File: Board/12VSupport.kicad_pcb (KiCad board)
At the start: 2 copper layers, 106.7 x 123.2 mm, 87 parts, among them J1 12V, J2 BATT, J3 BUCK_IN, J4 BUCK_OUT, J5 BOOST_IN, J6 BOOST_OUT, J7 TMP36GZ, J8 HEATER, J9 ICSP, K1 SLA-05VDC-SL-C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

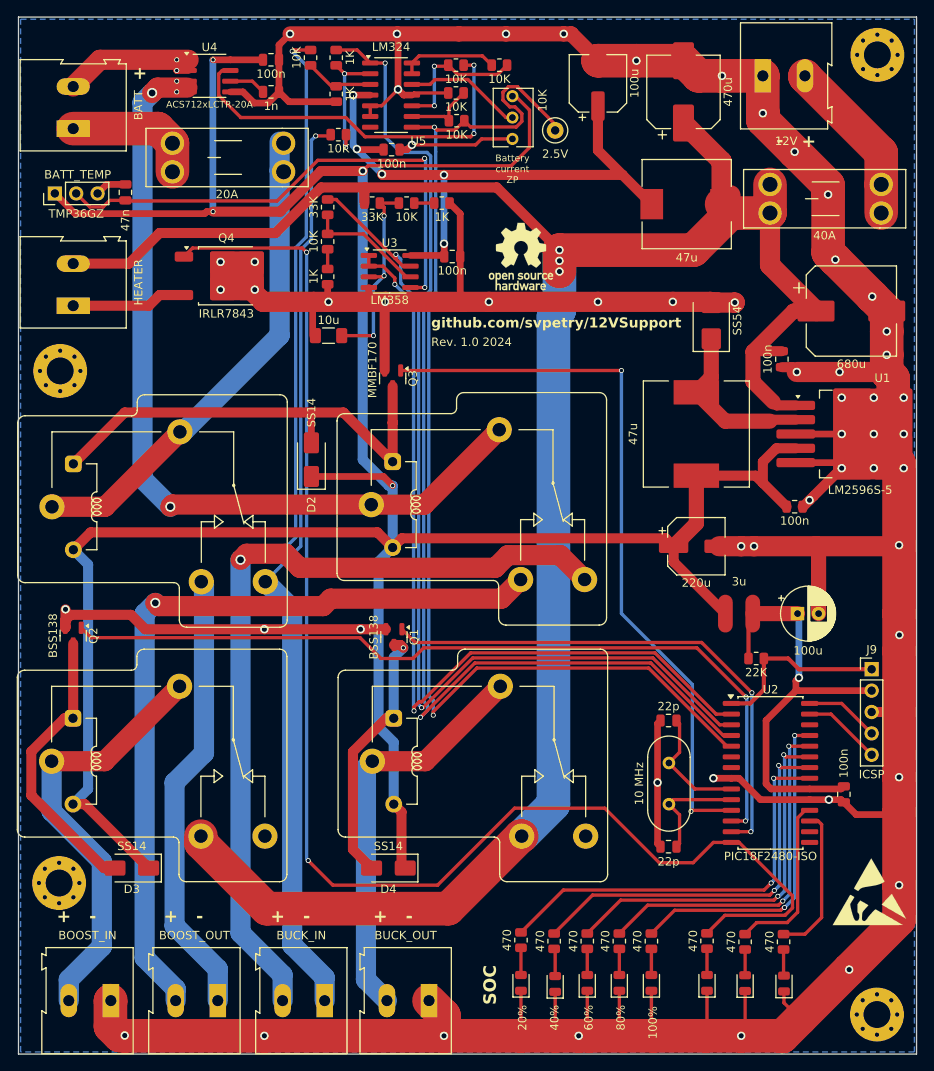
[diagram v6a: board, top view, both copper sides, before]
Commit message: Layout improvements. Set version to 1.1
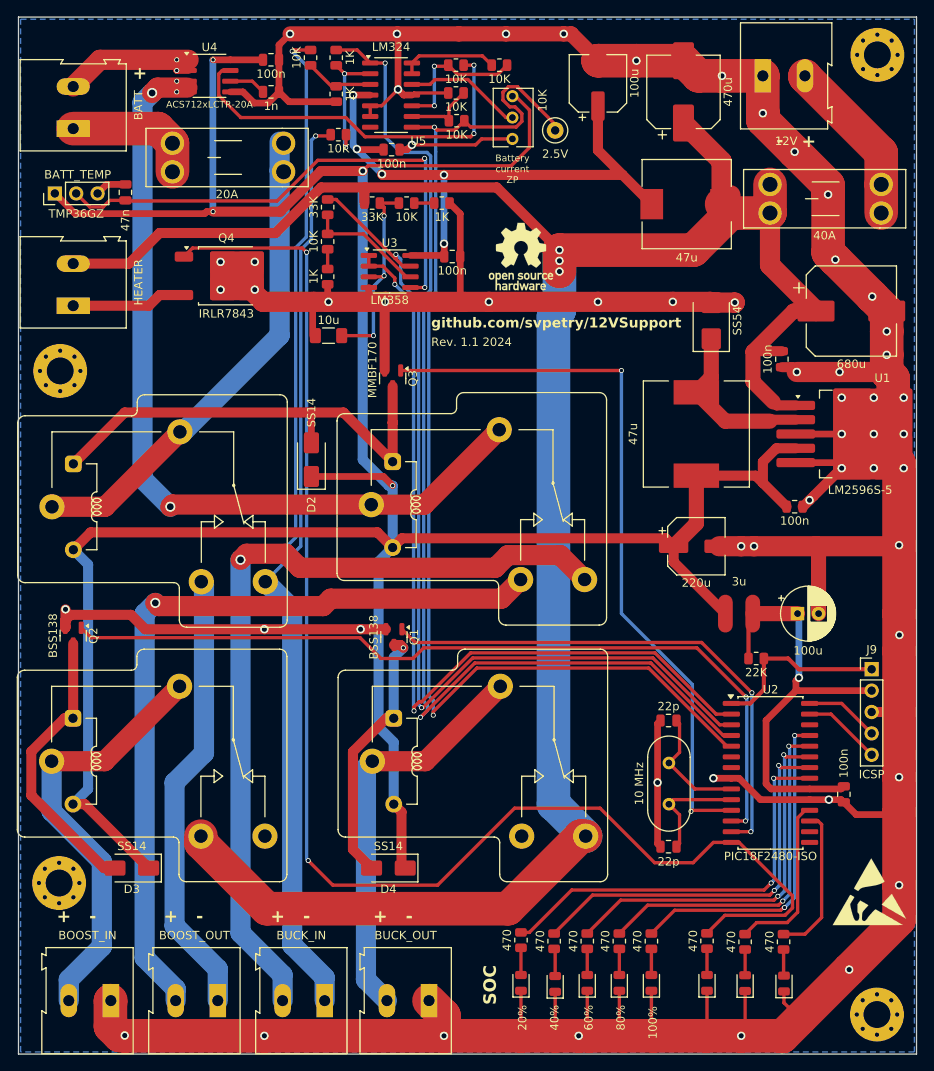
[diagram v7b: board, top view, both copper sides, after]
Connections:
- K4 pad 12: unconnected-(K4-Pad12) -> +12V
- K4 pad 14: +12V -> unconnected-(K4-Pad14)
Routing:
- net +12V: track 267.8 -> 275.4 mm
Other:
- board text added: "Rev. 1.1 2024"
- board text removed: "Rev. 1.0 2024"
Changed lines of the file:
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@@
 	(title_block
 		(date "2024-12-11")
-		(rev "1.0")
+		(rev "1.1")
 	)
 	(layers
@@
 	(net 36 "Net-(K2-Pad11A)")
 	(net 37 "unconnected-(K3-Pad12)")
-	(net 38 "unconnected-(K4-Pad12)")
+	(net 38 "unconnected-(K4-Pad14)")
 	(net 39 "REL_BUCK_OUT")
 	(net 40 "REL_BOOST_IN")
@@
 			(layers "*.Cu" "*.Mask")
 			(remove_unused_layers no)
-			(net 38 "unconnected-(K4-Pad12)")
-			(pintype "passive+no_connect")
+			(net 3 "+12V")
+			(pintype "passive")
 		)
 		(pad "14" thru_hole circle
@@
 			(layers "*.Cu" "*.Mask")
 			(remove_unused_layers no)
-			(net 3 "+12V")
-			(pintype "passive")
+			(net 38 "unconnected-(K4-Pad14)")
+			(pintype "passive+no_connect")
 		)
 		(pad "A1" thru_hole roundrect
@@
 		)
 	)
-	(gr_text "Rev. 1.0 2024"
+	(gr_text "Rev. 1.1 2024"
 		(at 90.932 80.518 0)
 		(layer "F.SilkS")
@@
 	)
 	(segment
-		(start 63.585 140.0055)
-		(end 63.585 139.21)
+		(start 71.4075 147.828)
+		(end 100.076 147.828)
 		(width 4)
 		(layer "F.Cu")
@@
 	)
 	(segment
-		(start 71.4075 147.828)
-		(end 63.585 140.0055)
-		(width 4)
-		(layer "F.Cu")
-		(net 3)
-	)
-	(segment
 		(start 55.038 71.2)
 		(end 58.674 67.564)
@@
 	)
 	(segment
+		(start 108.694 139.21)
+		(end 109.285 139.21)
+		(width 4)
+		(layer "F.Cu")
+		(net 3)
+	)
+	(segment
 		(start 131.185 65.193)
 		(end 126.493 65.193)
@@
 	)
 	(segment
+		(start 100.076 147.828)
+		(end 108.694 139.21)
+		(width 4)
+		(layer "F.Cu")
+		(net 3)
+	)
+	(segment
 		(start 83.011 62.2)
 		(end 83.011 64.008)
@@
 	)
 	(segment
-		(start 101.685 139.21)
-		(end 101.582 139.21)
-		(width 4)
-		(layer "F.Cu")
-		(net 3)
-	)
-	(segment
 		(start 126.493 65.193)
 		(end 122.09 69.596)
@@
 	)
 	(segment
+		(start 63.585 140.0055)
+		(end 71.4075 147.828)
+		(width 4)
+		(layer "F.Cu")
+		(net 3)
+	)
+	(segment
+		(start 63.585 139.21)
+		(end 63.585 140.0055)
+		(width 4)
+		(layer "F.Cu")
+		(net 3)
+	)
+	(segment
 		(start 72.448148 67.564)
 		(end 77.859148 62.153)
@@
 	)
 	(segment
-		(start 101.582 139.21)
-		(end 92.964 147.828)
-		(width 4)
-		(layer "F.Cu")
-		(net 3)
-	)
-	(segment
-		(start 92.964 147.828)
-		(end 71.4075 147.828)
-		(width 4)
-		(layer "F.Cu")
-		(net 3)
-	)
-	(segment
 		(start 106.172 72.136)
 		(end 106.172 69.596)
@@
 	)
 	(segment
+		(start 105.512 135.437)
+		(end 109.285 139.21)
+		(width 4)
+		(layer "B.Cu")
+		(net 3)
+	)
+	(segment
 		(start 106.172 76.708)
 		(end 106.172 69.596)
@@
 	)
 	(segment
-		(start 101.685 139.21)
-		(end 105.458 135.437)
+		(start 105.458 135.437)
+		(end 105.512 135.437)
 		(width 4)
 		(layer "B.Cu")
@@
 	)
 	(segment
-		(start 124.46 139.954)
-		(end 126.59 139.954)
+		(start 125.8365 148.612)
+		(end 123.698 150.7505)
 		(width 0.4)
 		(layer "F.Cu")
@@
 	)
 	(segment
-		(start 125.8365 148.612)
-		(end 123.698 150.7505)
+		(start 91.694 145.034)
+		(end 100.838 135.89)
 		(width 0.4)
 		(layer "F.Cu")
@@
 	)
 	(segment
-		(start 127.508 139.954)
-		(end 133.858 146.304)
+		(start 124.46 139.954)
+		(end 126.59 139.954)
 		(width 0.4)
 		(layer "F.Cu")
@@
 	)
 	(segment
-		(start 62.5855 69.35)
-		(end 75.638 69.35)
+		(start 110.998 135.89)
+		(end 117.475 142.367)
 		(width 0.4)
 		(layer "F.Cu")
@@
 	)
 	(segment
-		(start 133.858 146.304)
-		(end 133.858 147.731972)
+		(start 127.508 139.954)
+		(end 133.858 146.304)
 		(width 0.4)
 		(layer "F.Cu")
@@
 	)
 	(segment
-		(start 61.5655 70.37)
-		(end 62.5855 69.35)
+		(start 62.5855 69.35)
+		(end 75.638 69.35)
 		(width 0.4)
 		(layer "F.Cu")
@@
 	)
 	(segment
-		(start 122.047 142.367)
-		(end 124.46 139.954)
+		(start 133.858 146.304)
+		(end 133.858 147.731972)
 		(width 0.4)
 		(layer "F.Cu")
@@
 	)
 	(segment
-		(start 132.977972 148.612)
-		(end 125.8365 148.612)
+		(start 61.5655 70.37)
+		(end 62.5855 69.35)
 		(width 0.4)
 		(layer "F.Cu")
@@
 	)
 	(segment
-		(start 118.031834 142.367)
-		(end 122.047 142.367)
+		(start 132.977972 148.612)
+		(end 125.8365 148.612)
 		(width 0.4)
 		(layer "F.Cu")
@@
 	)
 	(segment
-		(start 75.638 69.35)
-		(end 76.138 69.85)
+		(start 100.838 135.89)
+		(end 110.998 135.89)
 		(width 0.4)
 		(layer "F.Cu")
@@
 	)
 	(segment
-		(start 111.554834 135.89)
-		(end 118.031834 142.367)
+		(start 76.327 142.113)
+		(end 79.248 145.034)
 		(width 0.4)
 		(layer "F.Cu")
@@
 	)
 	(segment
-		(start 79.248 145.034)
-		(end 91.694 145.034)
+		(start 75.638 69.35)
+		(end 76.138 69.85)
 		(width 0.4)
 		(layer "F.Cu")
@@
 	)
 	(segment
-		(start 91.694 145.034)
-		(end 100.838 135.89)
+		(start 117.475 142.367)
+		(end 122.047 142.367)
 		(width 0.4)
 		(layer "F.Cu")
@@
 	)
 	(segment
-		(start 100.838 135.89)
-		(end 111.554834 135.89)
+		(start 122.047 142.367)
+		(end 124.46 139.954)
 		(width 0.4)
 		(layer "F.Cu")
@@
 	)
 	(segment
-		(start 76.327 142.113)
-		(end 79.248 145.034)
+		(start 79.248 145.034)
+		(end 91.694 145.034)
 		(width 0.4)
 		(layer "F.Cu")
@@
 	)
 	(segment
-		(start 106.635 145.612)
+		(start 130.486 145.612)
+		(end 107.626 145.612)
+		(width 0.4)
+		(layer "F.Cu")
+		(net 49)
+	)
+	(segment
+		(start 102.591 150.647)
 		(end 101.6 150.647)
 		(width 0.4)
@@
 	)
 	(segment
-		(start 135.89 132.334)
-		(end 131.612 132.334)
+		(start 131.318 144.78)
+		(end 130.486 145.612)
 		(width 0.4)
 		(layer "F.Cu")
@@
 	)
 	(segment
-		(start 130.486 145.612)
-		(end 106.635 145.612)
+		(start 107.626 145.612)
+		(end 102.591 150.647)
 		(width 0.4)
 		(layer "F.Cu")
@@
 	)
 	(segment
-		(start 131.318 144.78)
-		(end 130.486 145.612)
+		(start 135.89 132.334)
+		(end 131.612 132.334)
 		(width 0.4)
 		(layer "F.Cu")

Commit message: WIP
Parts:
- removed REF** (x4): MountingHole_3.2mm_M3_Pad_Via, MountingHole:MountingHole_3.2mm_M3_Pad_Via
- removed REF**: ESD-Logo_8.9x8mm_SilkScreen, Symbol:ESD-Logo_8.9x8mm_SilkScreen
- removed REF**: OSHW-Logo_7.5x8mm_SilkScreen, Symbol:OSHW-Logo_7.5x8mm_SilkScreen
- added Q5: NCE30P30K, Package_TO_SOT_SMD:TO-252-2, F.Cu at (48.3, 114.8)
- added Q6: BSS138, Package_TO_SOT_SMD:SOT-23, F.Cu at (77.2, 115.6)
- added R24: 10K, Resistor_SMD:R_0805_2012Metric, F.Cu at (56.9, 114.6)
- moved Q2 30.0 mm to (77.3, 123.6)
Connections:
- net Net-(J4-Pin_2) renamed /BUCK_OUT+
- net Net-(J5-Pin_2) renamed /BOOST_IN+
- U2 pad 12: REL_BOOST_IN -> EN_BOOST_IN
- U2 pad 15: unconnected-(U2-SDI/SDA/RC4-Pad15) -> REL_BOOST_IN
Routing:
- net EN_BOOST_IN: track 0.00 -> 72.9 mm, vias 0 -> 2
- net +12V: track 275.4 -> 314.9 mm, vias 3 -> 4
- net GND: track 615.6 -> 585.1 mm, vias 55 -> 54
- net Net-(Q5-G): track 0.00 -> 28.3 mm
- net Net-(D3-A): track 34.2 -> 62.5 mm
- net /BOOST_IN+: track 51.4 -> 65.9 mm, vias 0 -> 4
- net REL_HEATER: track 169.2 -> 155.5 mm, vias 2 -> 4
- net REL_BOOST_IN: track 100.0 -> 90.8 mm, vias 2 -> 0
- net Net-(U2-RX/DT/RC7): track 20.3 -> 26.3 mm
- net Net-(D4-A): track 31.3 -> 29.9 mm, vias 1 -> 0
- net Net-(U2-TX/CK/RC6): track 18.0 -> 18.7 mm
